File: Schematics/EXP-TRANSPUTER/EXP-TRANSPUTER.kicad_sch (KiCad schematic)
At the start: 1 part, among them J1 DIN41612_03x32_ABC_Male_Hor

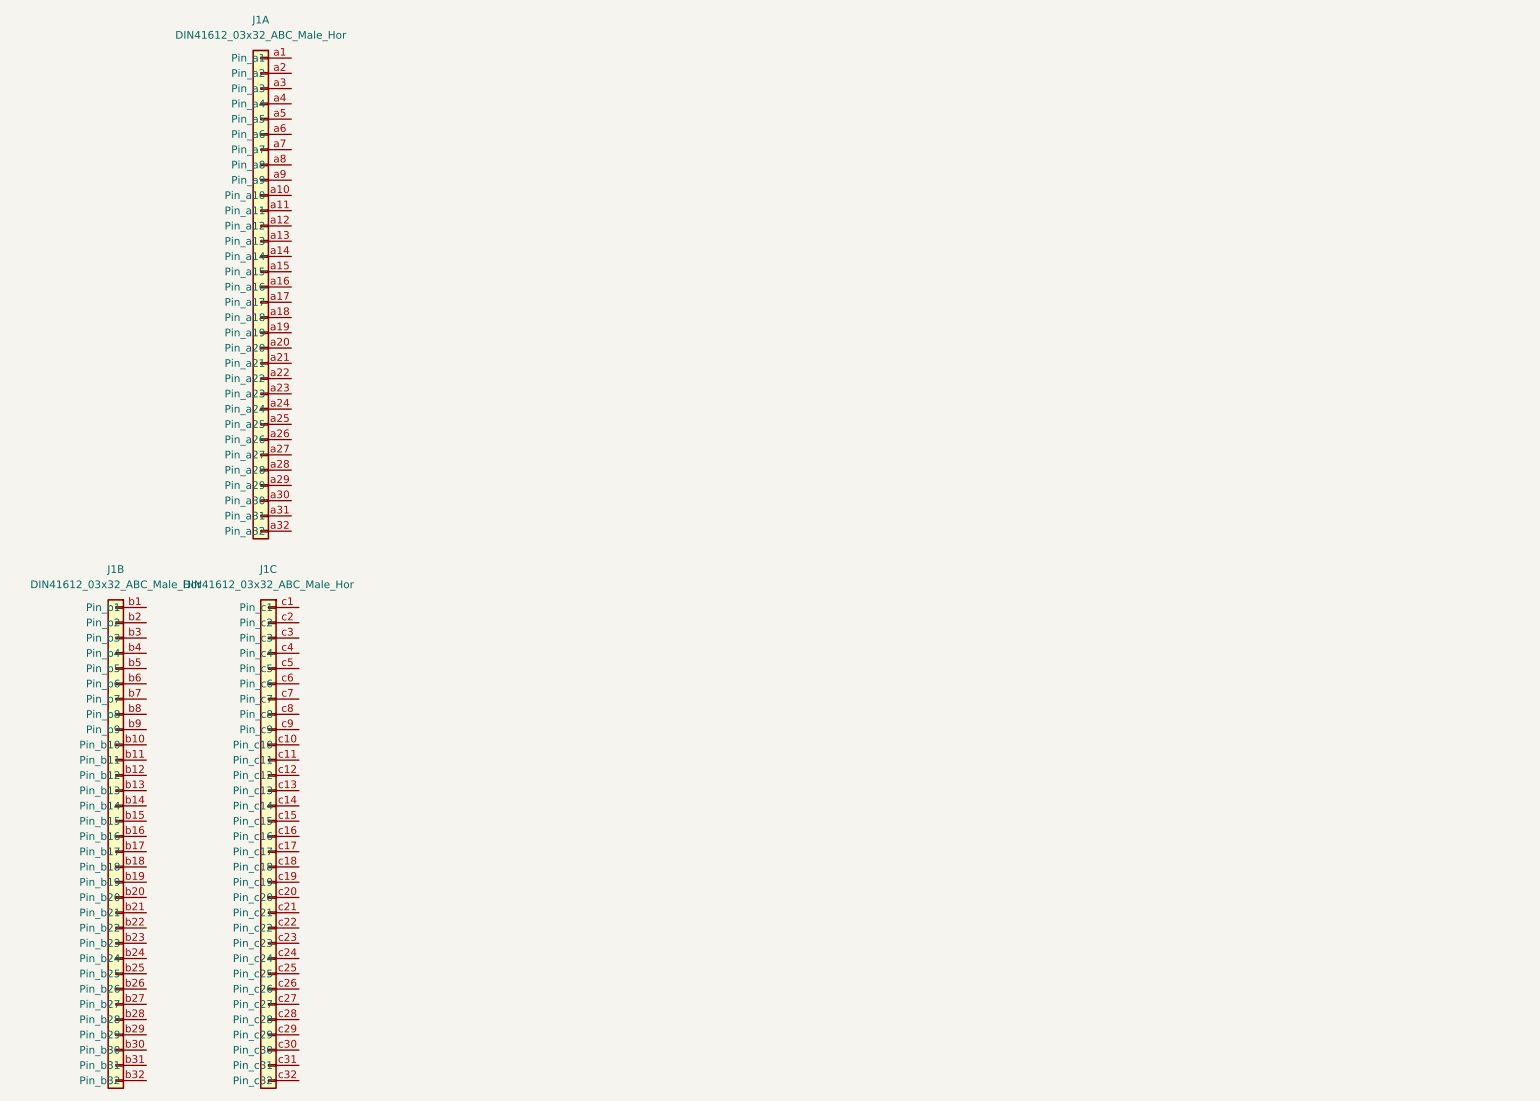
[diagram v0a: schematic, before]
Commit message: Begun work on transputer expansion board
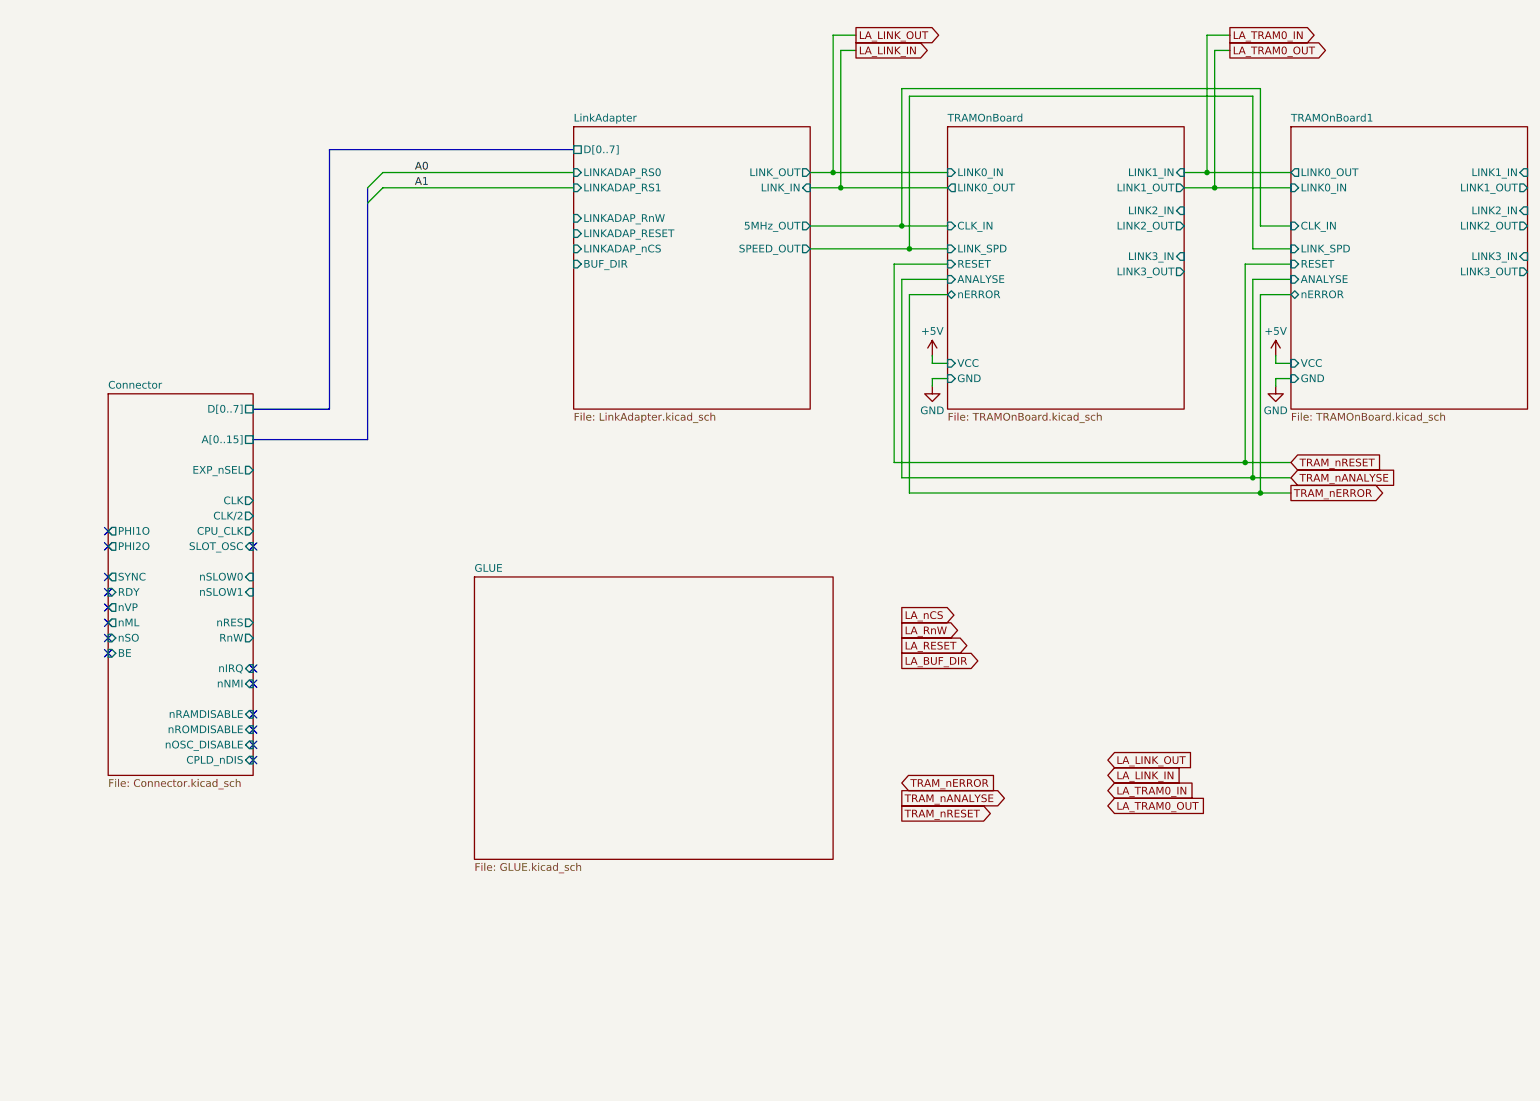
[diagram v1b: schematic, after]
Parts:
- removed J1: DIN41612_03x32_ABC_Male_Hor, Connector_DIN:DIN41612_C_3x32_Male_Horizontal_THT, symbol Jayne k7:DIN41612_03x32_ABC_Male_Hor
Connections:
- no-connect marks 0 -> 15
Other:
- added sheet Connector (Connector.kicad_sch)
- added sheet GLUE (GLUE.kicad_sch)
- added sheet LinkAdapter (LinkAdapter.kicad_sch)
- added sheet TRAMOnBoard (TRAMOnBoard.kicad_sch)
- added sheet TRAMOnBoard1 (TRAMOnBoard.kicad_sch)
